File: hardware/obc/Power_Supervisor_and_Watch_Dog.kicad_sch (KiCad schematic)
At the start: 21 parts, among them Q103 IRF7306, Q105 NPN, Q106 MBT2222ADW1T1, Q107 MBT2222ADW1T1

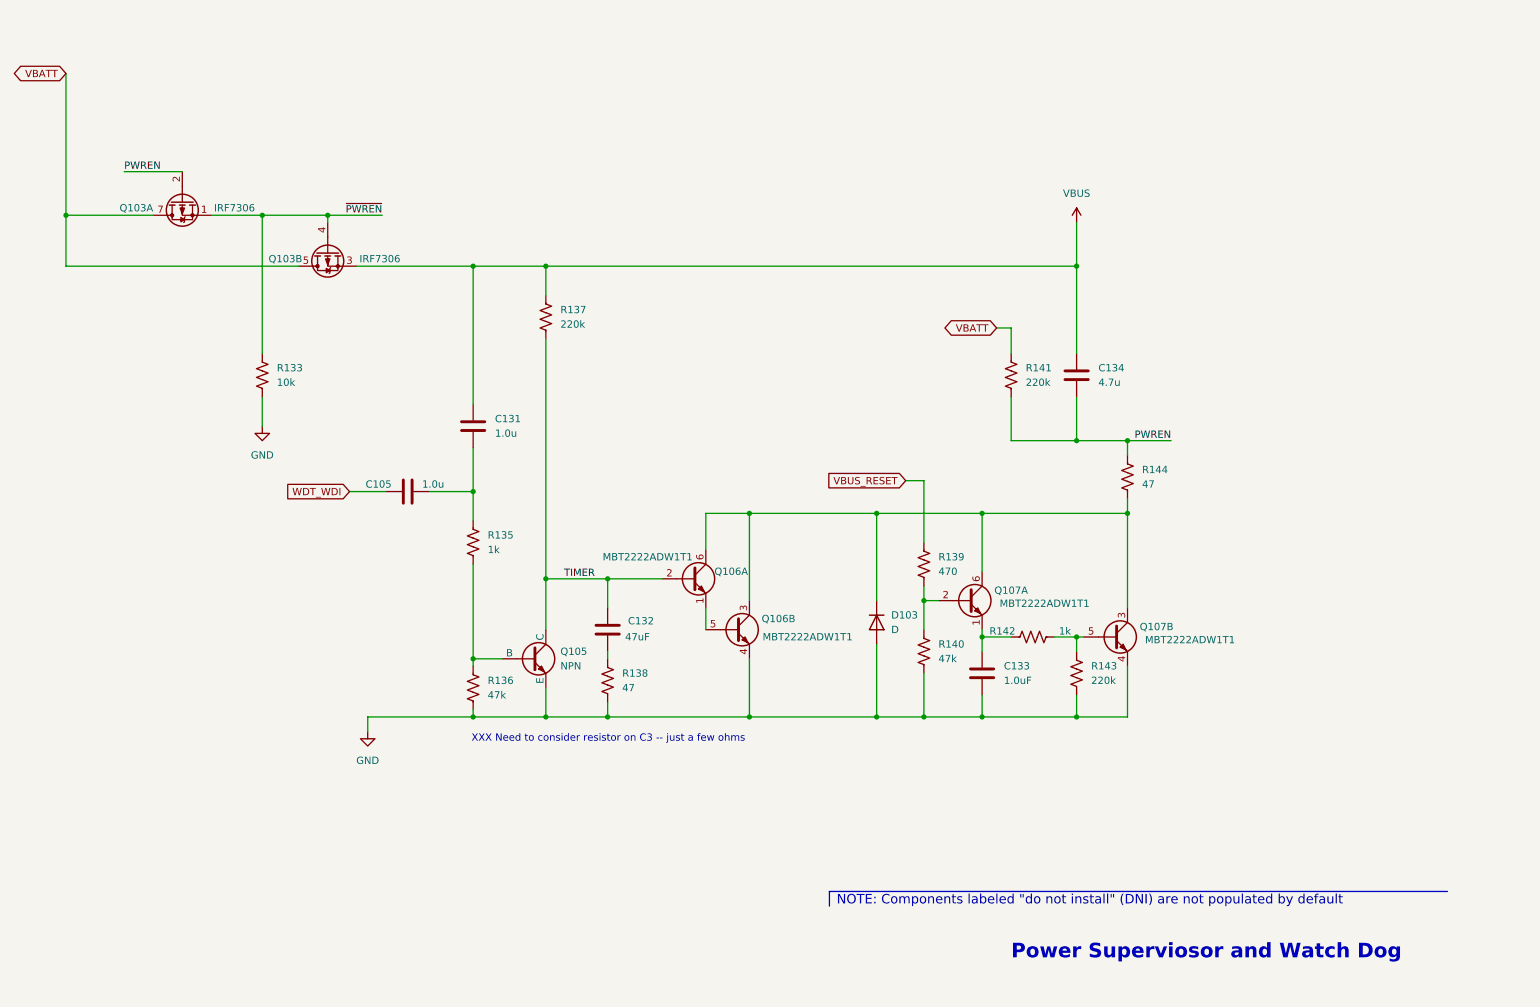
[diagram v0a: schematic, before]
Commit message: obc: power sup: fix mistake, add theory, clean up
1. During component selection, FET drain and sources were reversed
   (fixed).
2. Was able to make page much cleaner.
3. Rearrange power page, add some XXX comments.
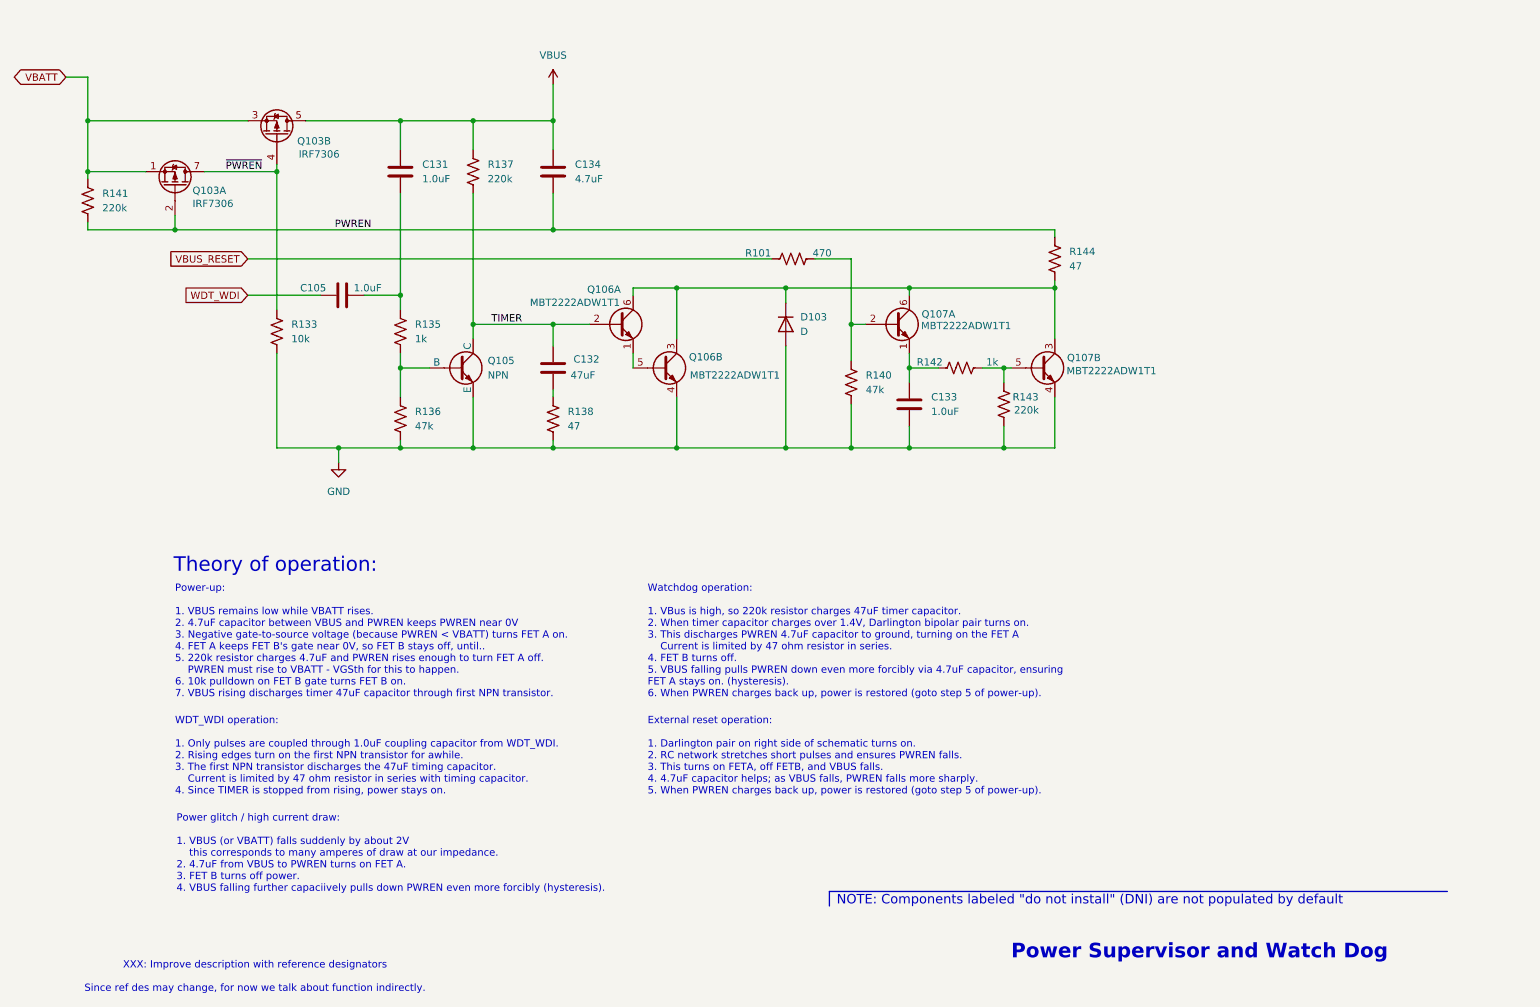
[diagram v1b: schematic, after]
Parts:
- removed R139: 470, symbol Device:R_US
- added R101: 470, symbol Device:R_US
- C105, C131: value 1.0u -> 1.0uF
- C134: value 4.7u -> 4.7uF
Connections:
- net VBATT: now also Q103.1 (S1), Q103.3 (S2); no longer Q103.5 (D2), Q103.6 (D2), Q103.7 (D1), Q103.8 (D1)
- net VBUS: now also Q103.5 (D2), Q103.6 (D2); no longer Q103.3 (S2)
- net VBUS_RESET: now also R101.1
- net ~{PWREN}: now also Q103.7 (D1), Q103.8 (D1); no longer Q103.1 (S1)
- net at Q107.2 (B1), R140.1: now also R101.2
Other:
- note added: "External reset operation: 1. Darlington pair on right side of schematic turns on. 2. RC network stretches short pulses and ensures PWREN falls. 3. This turns on FETA, off FETB, and VBUS falls. 4. 4.7uF capacitor helps; as VBUS falls, PWREN falls more sharply. 5. When PWREN charges back up, power is restored (goto step 5 of power-up)."
- note added: "Power Supervisor and Watch Dog"
- note added: "Power glitch / high current draw: 1. VBUS (or VBATT) falls suddenly by about 2V this corresponds to many amperes of draw at our impedance. 2. 4.7uF from VBUS to PWREN turns on FET A. 3. FET B turns off power. 4. VBUS falling further capaciively pulls down PWREN even more forcibly (hysteresis)."
- note added: "Power-up: 1. VBUS remains low while VBATT rises. 2. 4.7uF capacitor between VBUS and PWREN keeps PWREN near 0V 3. Negative gate-to-source voltage (because PWREN < VBATT) turns FET A on. 4. FET A keeps FET B's gate near 0V, so FET B stays off, until.. 5. 220k resistor charges 4.7uF and PWREN rises enough to turn FET A off. PWREN must rise to VBATT - VGSth for this to happen. 6. 10k pulldown on FET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"
- note added: "Theory of operation:"
- note added: "WDT_WDI operation: 1. Only pulses are coupled through 1.0uF coupling capacitor from WDT_WDI. 2. Rising edges turn on the first NPN transistor for awhile. 3. The first NPN transistor discharges the 47uF timing capacitor. Current is limited by 47 ohm resistor in series with timing capacitor. 4. Since TIMER is stopped from rising, power stays on."
- note added: "Watchdog operation: 1. VBus is high, so 220k resistor charges 47uF timer capacitor. 2. When timer capacitor charges over 1.4V, Darlington bipolar pair turns on. 3. This discharges PWREN 4.7uF capacitor to ground, turning on the FET A Current is limited by 47 ohm resistor in series. 4. FET B turns off. 5. VBUS falling pulls PWREN down even more forcibly via 4.7uF capacitor, ensuring FET A stays on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"
- note added: "XXX: Improve description with reference designators Since ref des may change, for now we talk about function indirectly."
- note removed: "Power Superviosor and Watch Dog"
- note removed: "XXX Need to consider resistor on C3 -- just a few ohms"
- moved on the sheet: C105, C131, C132, C133, C134, D103, Q103A, Q103B, Q105, Q106A, Q106B, Q107A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

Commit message: OBC: Freed up GPIO0 and added footprints
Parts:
- C105, C131, C132, C133, C134: footprint (none) -> Capacitor_SMD:C_0603_1608Metric
- R101, R133, R135, R136, R137, R138, R140, R141, R142, R143, R144: footprint (none) -> Resistor_SMD:R_0603_1608Metric
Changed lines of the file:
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@@
 			)
 		)
-		(property "Footprint" ""
+		(property "Footprint" "Resistor_SMD:R_0603_1608Metric"
 			(at 181.864 76.454 90)
 			(effects
@@
 			)
 		)
-		(property "Footprint" ""
+		(property "Footprint" "Resistor_SMD:R_0603_1608Metric"
 			(at 84.836 71.374 90)
 			(effects
@@
 			)
 		)
-		(property "Footprint" ""
+		(property "Footprint" "Capacitor_SMD:C_0603_1608Metric"
 			(at 77.47 63.8048 0)
 			(effects
@@
 			)
 		)
-		(property "Footprint" ""
+		(property "Footprint" "Capacitor_SMD:C_0603_1608Metric"
 			(at 82.8548 39.37 0)
 			(effects
@@
 			)
 		)
-		(property "Footprint" ""
+		(property "Footprint" "Capacitor_SMD:C_0603_1608Metric"
 			(at 171.7548 80.01 0)
 			(effects
@@
 			)
 		)
-		(property "Footprint" ""
+		(property "Footprint" "Resistor_SMD:R_0603_1608Metric"
 			(at 28.194 48.006 90)
 			(effects
@@
 			)
 		)
-		(property "Footprint" ""
+		(property "Footprint" "Resistor_SMD:R_0603_1608Metric"
 			(at 111.506 86.614 90)
 			(effects
@@
 			)
 		)
-		(property "Footprint" ""
+		(property "Footprint" "Resistor_SMD:R_0603_1608Metric"
 			(at 63.246 71.374 90)
 			(effects
@@
 			)
 		)
-		(property "Footprint" ""
+		(property "Footprint" "Resistor_SMD:R_0603_1608Metric"
 			(at 95.504 42.926 90)
 			(effects
@@
 			)
 		)
-		(property "Footprint" ""
+		(property "Footprint" "Resistor_SMD:R_0603_1608Metric"
 			(at 152.654 57.404 90)
 			(effects
@@
 			)
 		)
-		(property "Footprint" ""
+		(property "Footprint" "Resistor_SMD:R_0603_1608Metric"
 			(at 163.576 80.264 90)
 			(effects
@@
 			)
 		)
-		(property "Footprint" ""
+		(property "Footprint" "Capacitor_SMD:C_0603_1608Metric"
 			(at 109.5248 39.37 0)
 			(effects
@@
 			)
 		)
-		(property "Footprint" ""
+		(property "Footprint" "Resistor_SMD:R_0603_1608Metric"
 			(at 199.136 58.674 90)
 			(effects
@@
 			)
 		)
-		(property "Footprint" ""
+		(property "Footprint" "Capacitor_SMD:C_0603_1608Metric"
 			(at 109.5248 73.66 0)
 			(effects
@@
 			)
 		)
-		(property "Footprint" ""
+		(property "Footprint" "Resistor_SMD:R_0603_1608Metric"
 			(at 82.804 86.106 90)
 			(effects
@@
 			)
 		)
-		(property "Footprint" ""
+		(property "Footprint" "Resistor_SMD:R_0603_1608Metric"
 			(at 188.214 83.566 90)
 			(effects

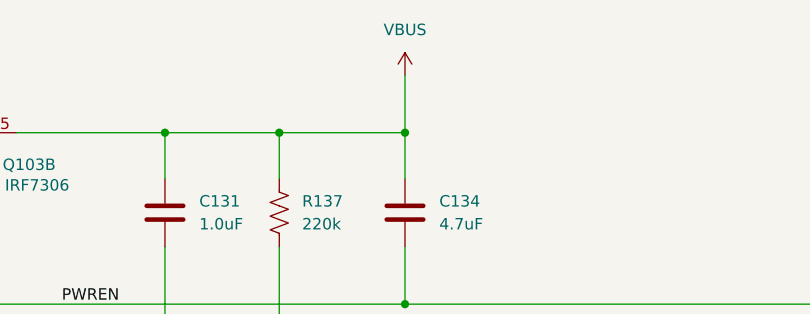
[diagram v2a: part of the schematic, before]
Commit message: obc: Changed RF and 3.3V regulators from VBATT to VWATCHEDRAIL
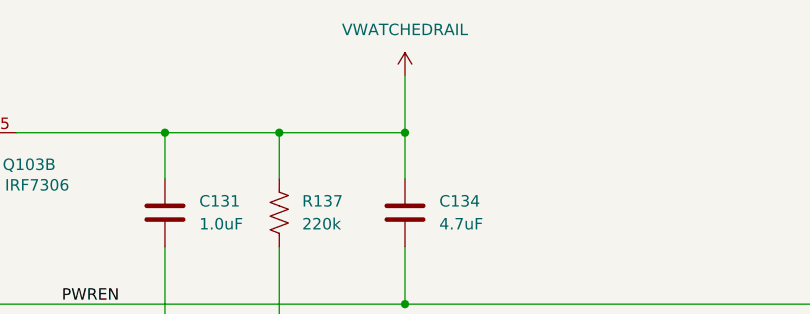
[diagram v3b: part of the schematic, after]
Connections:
- net VBUS renamed VWATCHEDRAIL
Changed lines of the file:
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@@
 			)
 		)
-		(property "Value" "VBUS"
+		(property "Value" "VWATCHEDRAIL"
 			(at 110.49 22.86 0)
 			(effects

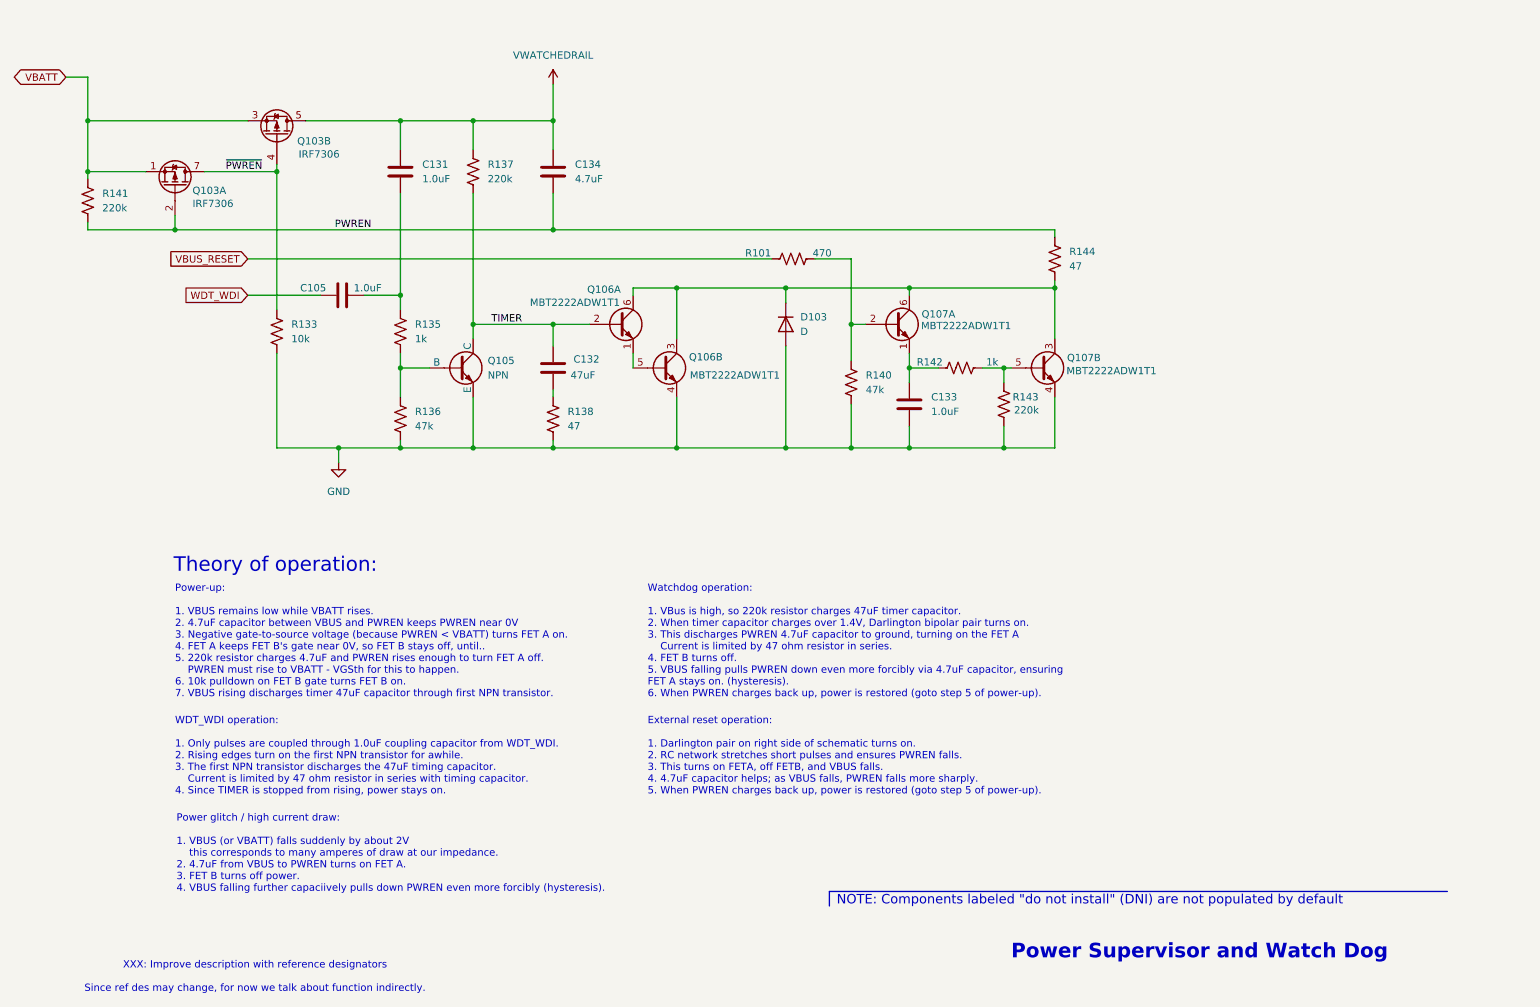
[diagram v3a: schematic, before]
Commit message: obc: Fixed errors from design review
- Gave proper attribution on all pages
- Spread out components on Avionics page
- Changed GPS power circuit
- Added a DNP resistor in between VBATT and VWATCHEDRAIL
- Added various other part numbers on Power Supervisor and Watch Dog Page
- Changed Power Supervisor and Watch Dog Page to page 3
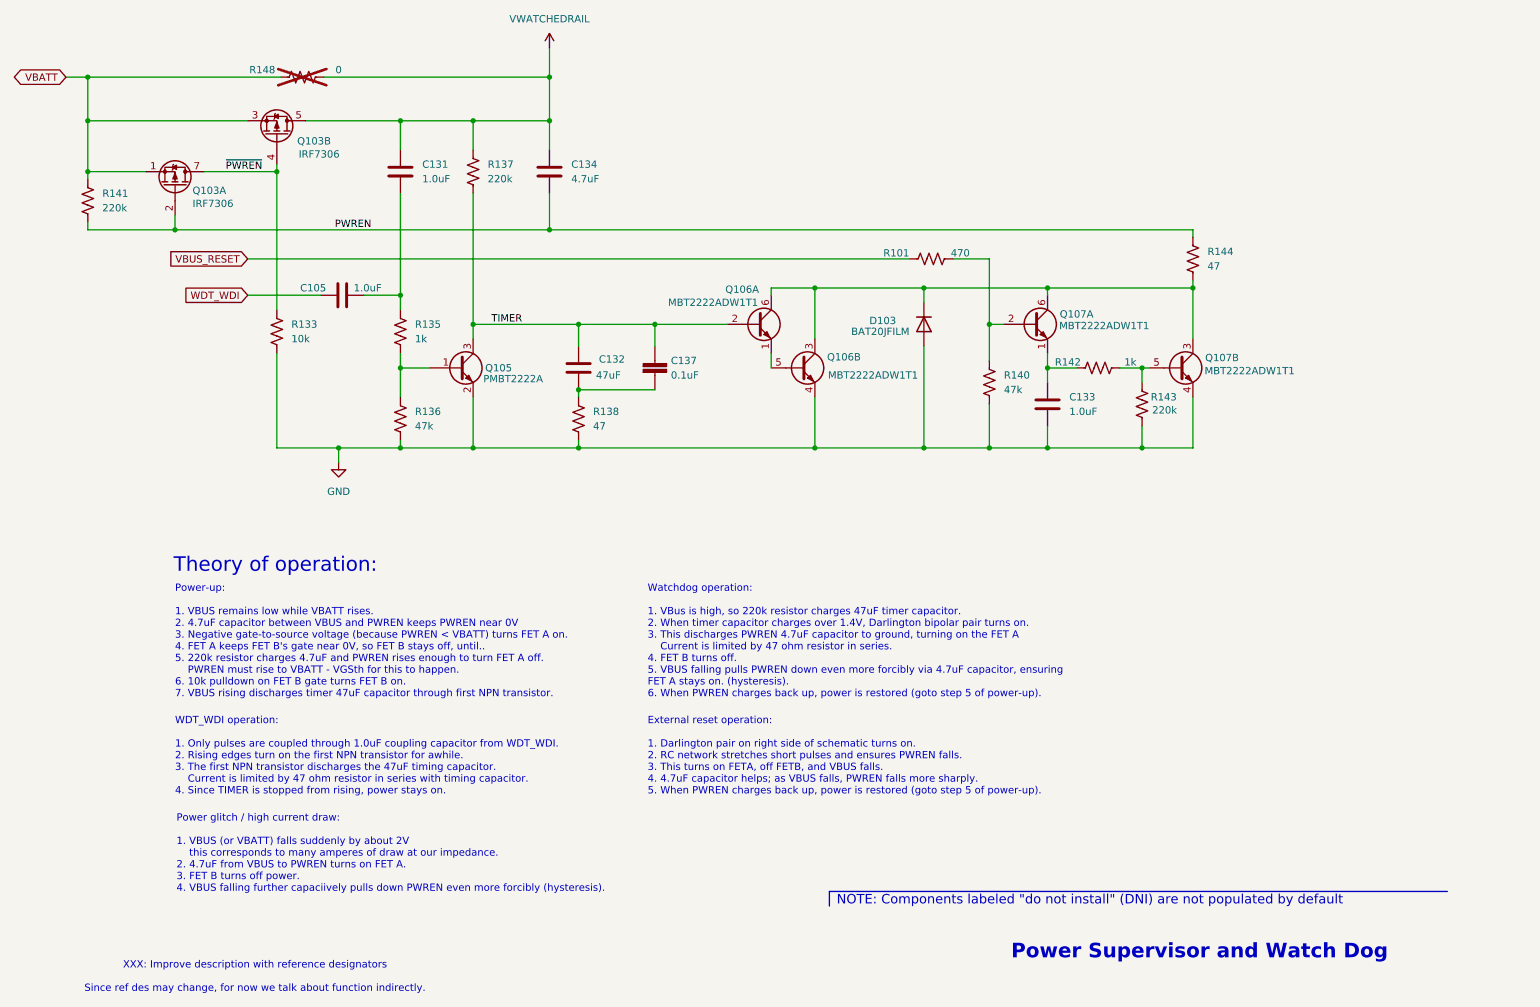
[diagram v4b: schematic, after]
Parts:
- removed Q105: NPN, symbol Simulation_SPICE:NPN
- added C137: 0.1uF, Capacitor_SMD:C_0603_1608Metric, symbol mainboard:0.1UF-0603-25V-5%
- added Q105: PMBT2222A, Package_TO_SOT_SMD:SOT-23, symbol Transistor_BJT:PMBT2222A
- added R148: 0, symbol Device:R_US
- C132: LCSC (none) -> C94034
- D103: value D -> BAT20JFILM; Manufacturer_Part_Number (none) -> BAT20JFILM
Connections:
- net GND: now also Q105.2 (E)
- net TIMER: now also C137.1, Q105.3 (C)
- net VBATT: now also R148.1
- net VWATCHEDRAIL: now also R148.2
- net at R135.2, R136.2: now also Q105.1 (B)
- net at C132.1, R138.1: now also C137.2
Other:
- company: Michael Lyle -> Luke Titi, Michael Lyle
- moved on the sheet: C132, C133, C134, D103, Q106A, Q106B, Q107A, Q107B, R101, R138, R140, R142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

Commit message: obc: Fixed second design review, and fixed up BOM
- added layout comments on schematic
- fixed various comments
- added many LCSC # for components
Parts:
- C105, C131, C133: LCSC (none) -> C59782
- C134: LCSC (none) -> C1705
- C137: LCSC (none) -> C1591
- D103: footprint (none) -> Diode_SMD:D_SOD-323
- R101: LCSC (none) -> C114669
- R133: LCSC (none) -> C169849
- R135, R142: LCSC (none) -> C844746
- R136, R138, R140, R144: LCSC (none) -> C105579
- R137, R141, R143: LCSC (none) -> C123420
- R148: footprint (none) -> Resistor_SMD:R_0603_1608Metric; LCSC (none) -> C100044

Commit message: obc: final cleanup before review
ex. cleaned wires in PCB, made text nicer on the schematic
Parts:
- D103: LCSC (none) -> C155590
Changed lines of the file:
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@@
+			)
+		)
+		(property "LCSC" "C155590"
+			(at 175.26 69.85 0)
+			(effects
+				(font
+					(size 1.27 1.27)
+				)
+				(hide yes)
 			)
 		)
